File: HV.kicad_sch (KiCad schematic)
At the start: 7 parts, among them J401 1935161, J402 1935161, Q401 MCB90N12A-TP, U401 LTV-816S

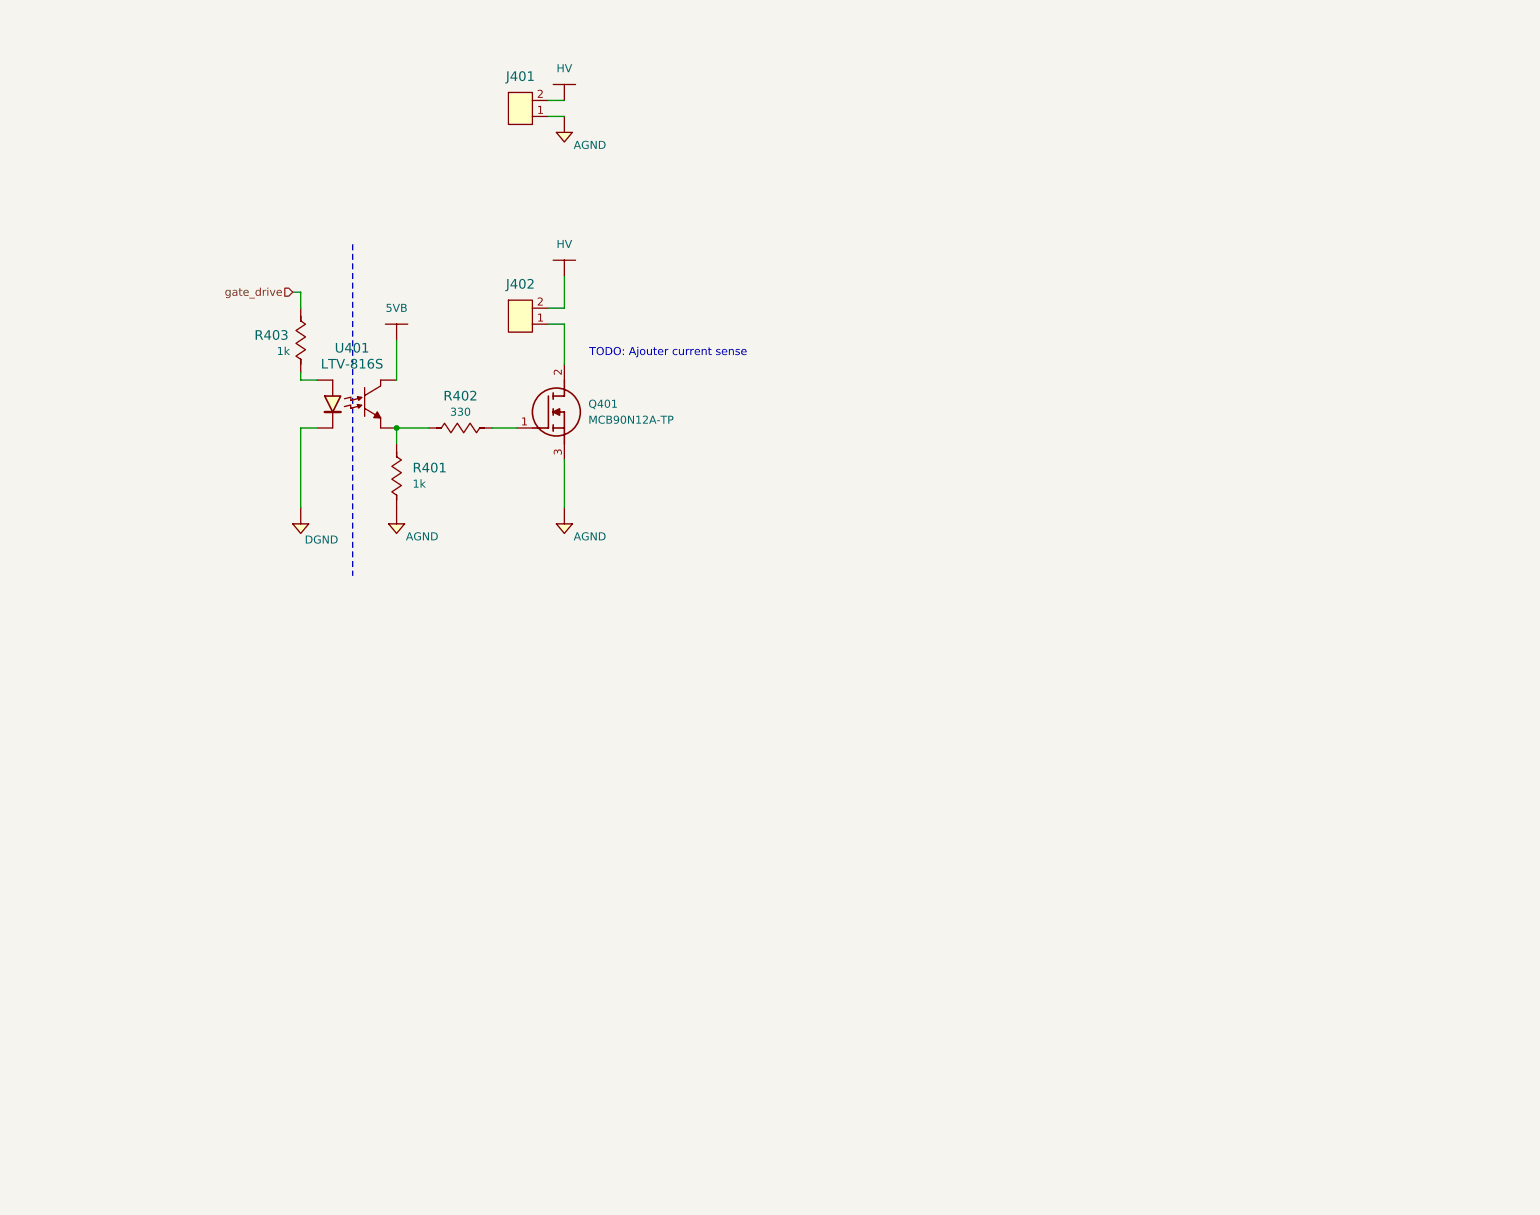
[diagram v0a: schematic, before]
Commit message: update schematic
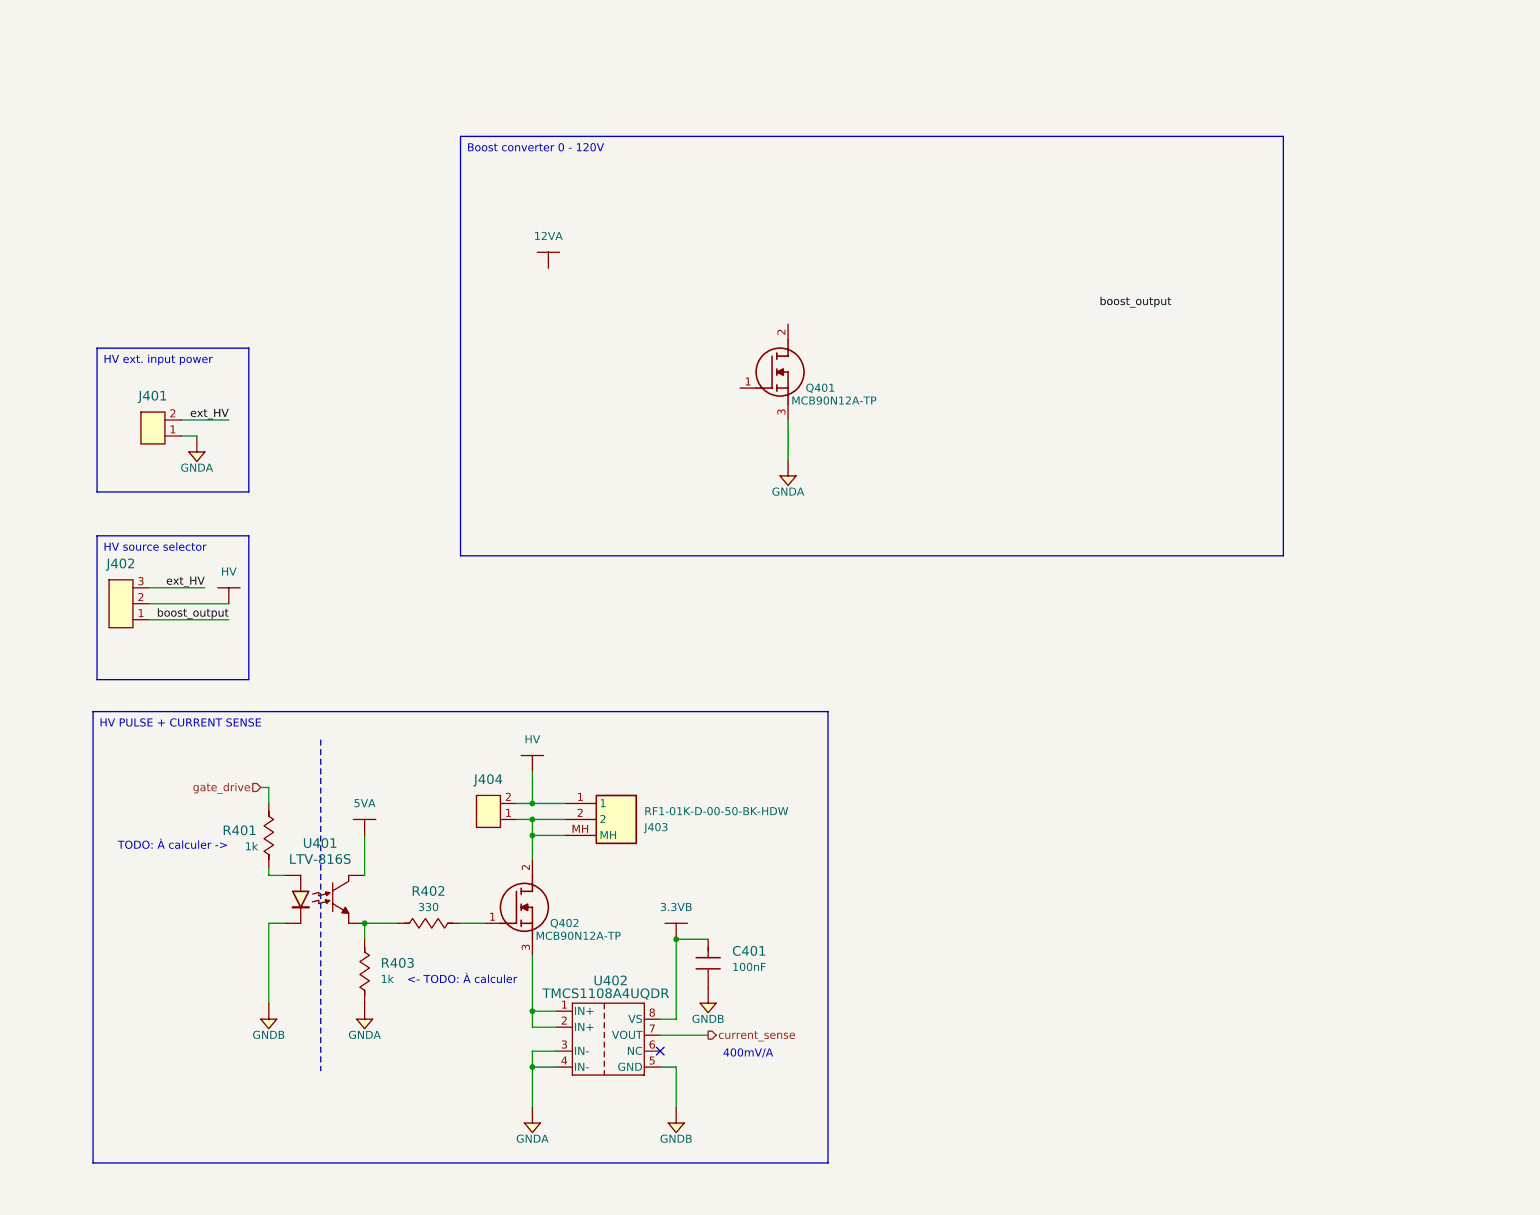
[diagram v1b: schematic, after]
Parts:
- added C401: 885012207098, Capacitors:C0805, symbol Capacitors:885012207098
- added J402: Header_Male_Pin_2.54mm_1X3_,_Unshrouded, Connectors:Headers_2.54mm_1X3, symbol Connectors:Header_Male_Pin_2.54mm_1X3_,_Unshrouded
- added J403: RF1-01K-D-00-50-BK-HDW, Connectors:RF101KD0050, symbol Connectors:RF1-01K-D-00-50-BK-HDW
- added Q401: MCB90N12A-TP, IC:MCB90N12ATP, symbol Transistors:MCB90N12A-TP
- added U402: TMCS1108A4UQDR, IC:SOIC-8, symbol Sensors:TMCS1108A4UQDR
- renumbered J402 to J404, Q401 to Q402, R403 to R401, R401 to R403
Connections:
- net HV: now also J402.2, J403.1; no longer J401.2
- net at J404.1, Q402.2 (D): now also J403.2, J403.MH
- net 5VB renamed 5VA
- net AGND renamed GNDA
- net GNDA: now also Q401.3 (S), U402.3 (IN-), U402.4 (IN-); no longer Q402.3 (S)
- net DGND renamed GNDB
- net GNDB: now also C401.1, U402.5 (GND)
- new net: Q402.3 (S), U402.1 (IN+), U402.2 (IN+)
- new net 3.3VB: C401.2, U402.8 (VS)
- new net boost_output: J402.1
- new net current_sense: U402.7 (VOUT)
- new net ext_HV: J401.2, J402.3
- no-connect marks 0 -> 1
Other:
- note added: "400mV/A"
- note added: "<- TODO: À calculer"
- note added: "TODO: À calculer ->"
- note removed: "TODO: Ajouter current sense"
- title: (none) -> HV
- moved on the sheet: J401, J404, Q402, R401, R402, R403, U401

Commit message: update schematic
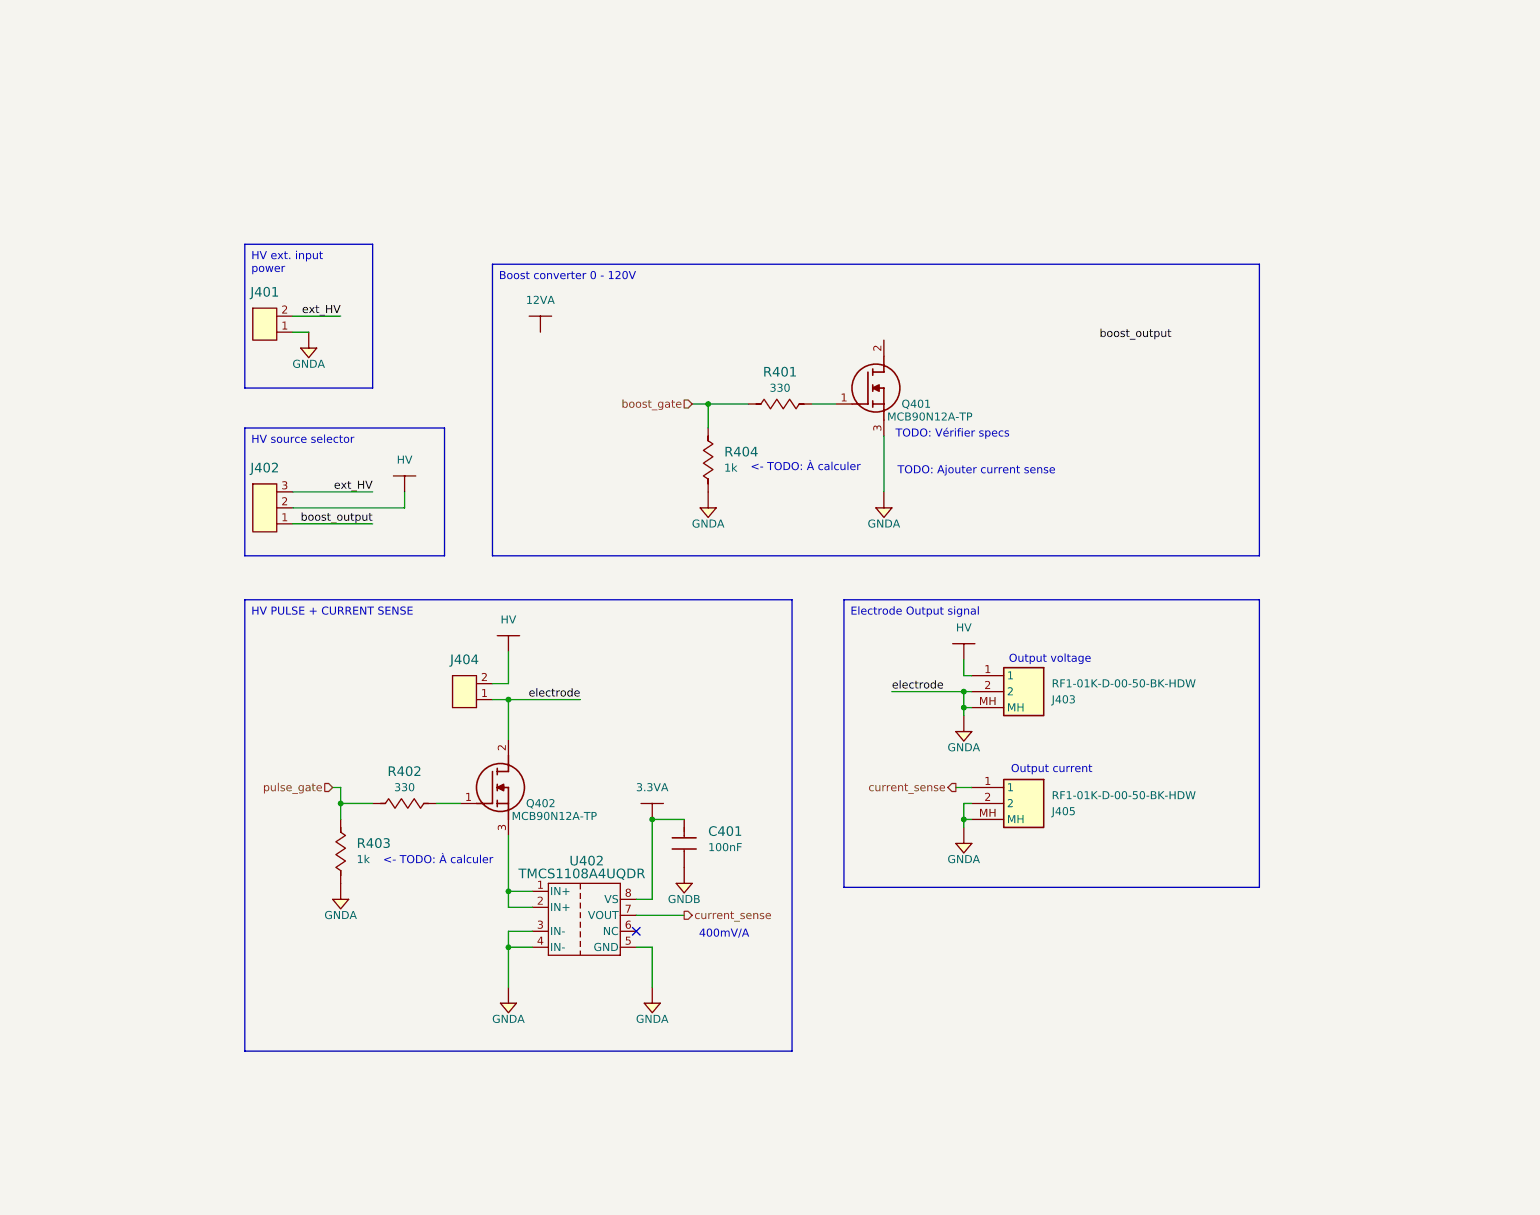
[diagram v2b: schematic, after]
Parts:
- removed R401: RC0805JR-071KL, Resistors:R0805, symbol Resistors:RC0805JR-071KL
- removed U401: LTV-816S, IC:4-SMD, symbol Isolators:LTV-816S
- added J405: RF1-01K-D-00-50-BK-HDW, Connectors:RF101KD0050, symbol Connectors:RF1-01K-D-00-50-BK-HDW
- added R401: RC0805JR-07330RL, Resistors:R0805, symbol Resistors:RC0805JR-07330RL
- added R404: RC0805JR-071KL, Resistors:R0805, symbol Resistors:RC0805JR-071KL
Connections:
- net GNDA: now also J403.2, J403.MH, J404.1, Q402.2 (D), U402.5 (GND), J405.2, J405.MH, R404.1
- net GNDB: no longer U402.5 (GND)
- net current_sense: now also J405.1
- net pulse_gate: now reaches R402.1, R403.2
- net at Q401.1 (G): now also R401.2
- net 3.3VB renamed 3.3VA
- new net boost_gate: R401.1, R404.2
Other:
- note added: "Output current"
- note added: "Output voltage"
- note added: "TODO: Ajouter current sense"
- note added: "TODO: Vérifier specs"
- note removed: "TODO: À calculer ->"
- moved on the sheet: C401, J401, J402, J404, Q401, Q402, R402, R403, U402

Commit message: update schematic
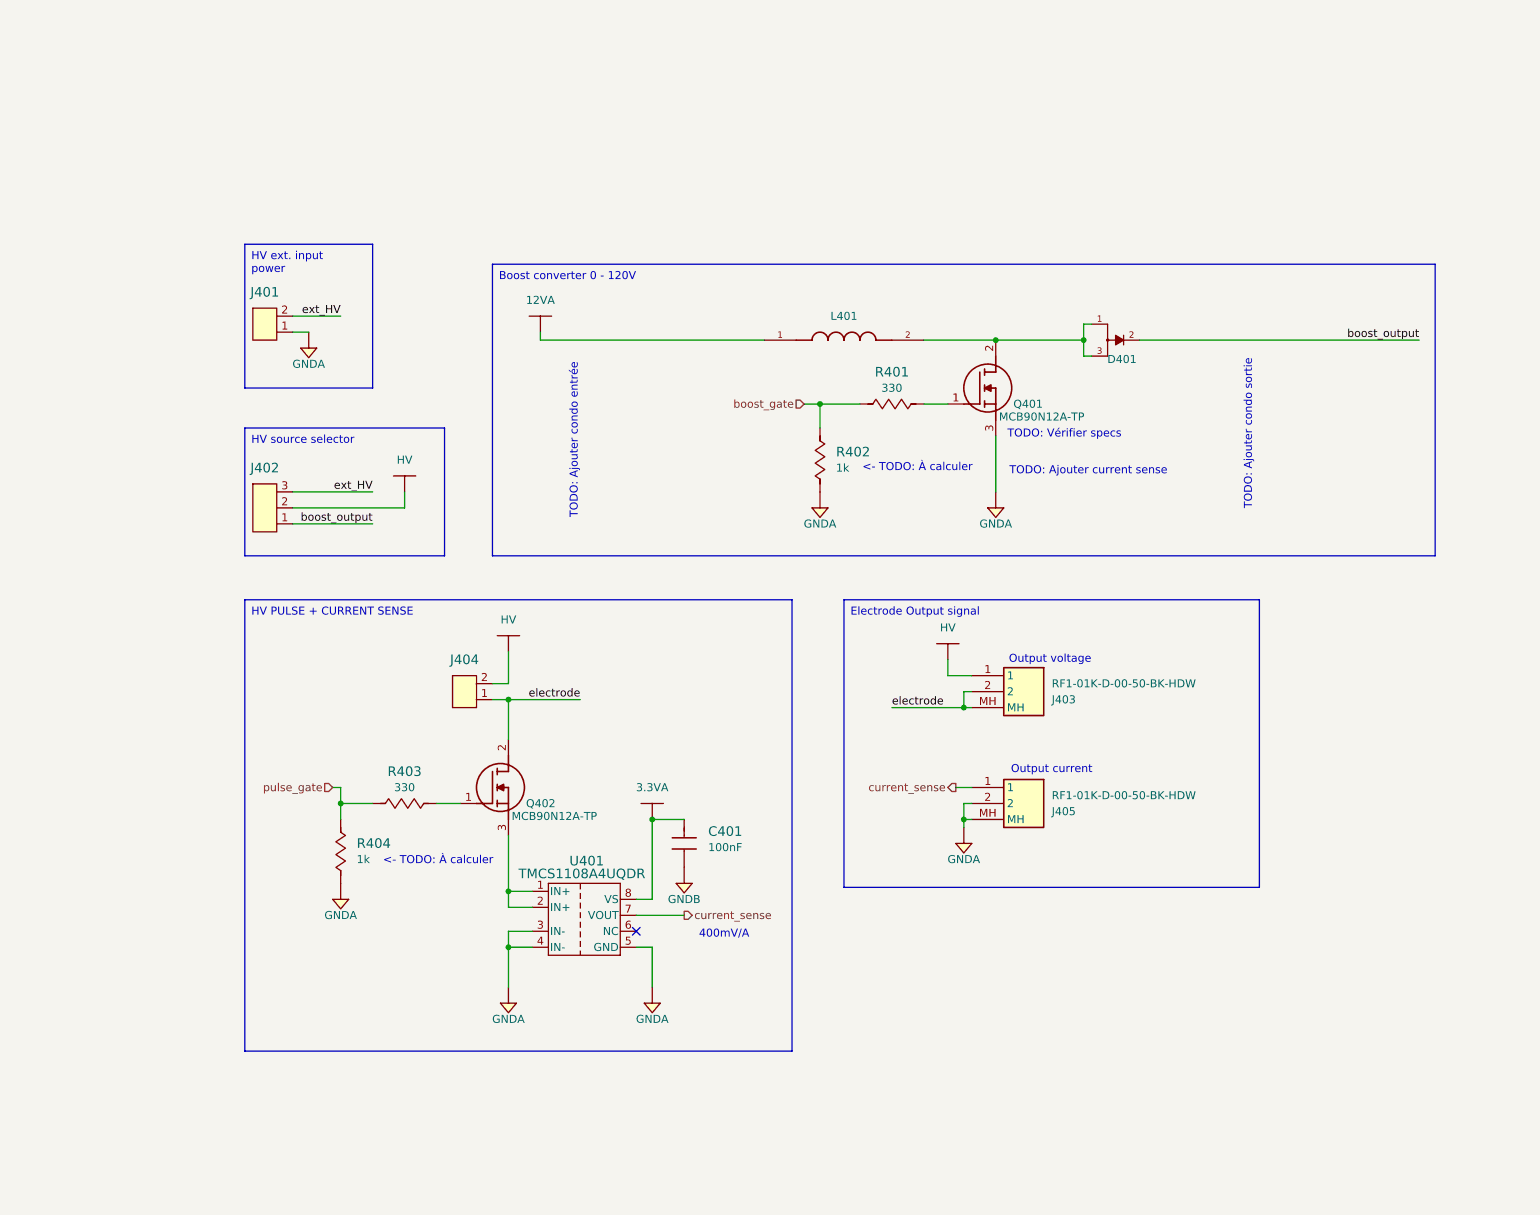
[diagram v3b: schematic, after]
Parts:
- added D401: SBRD10200TR, Diodes:DPAK228P1005X240-4N, symbol Diodes:SBRD10200TR
- added L401: ATCA-08-471M-H, Inductors:IND_ATCA-08-471M-H, symbol Inductors:ATCA-08-471M-H
- renumbered R404 to R402, R402 to R403, R403 to R404, U402 to U401
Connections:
- net 12VA: now also L401.1
- net GNDA: no longer J403.2, J403.MH, J404.1, Q402.2 (D)
- net boost_output: now also D401.2
- net at Q401.2 (D): now also D401.1, D401.3, L401.2
- new net electrode: J403.2, J403.MH, J404.1, Q402.2 (D)
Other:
- note added: "TODO: Ajouter condo entrée"
- note added: "TODO: Ajouter condo sortie"
- moved on the sheet: Q401, R401, R402

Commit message: modif schématique
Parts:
- added D401: SBRD10200TR, Diodes:DPAK228P1005X240-4N, symbol Diodes:SBRD10200TR
- added R403, R411: RMCF0805FT10M0, Resistors:R0805, symbol Resistors:RMCF0805FT10M0
- added R404, R405, R410, R412: RC0805FR-075K6L, Resistors:R0805, symbol Resistors:RC0805FR-075K6L
- added R406, R413: RC0805FR-07200KL, Resistors:R0805, symbol Resistors:RC0805FR-07200KL
- added R408: RC0805JR-071KL, Resistors:R0805, symbol Resistors:RC0805JR-071KL
- added TP401: Test_Point_THM, Connectors:Keystone_5001, symbol Connectors:Test_Point_THM
- added U401: MCP6L04T-E/SL, IC:SOIC127P600X175-14N, symbol Amplifiers:MCP6L04T-E/SL
- added U402: LTV-816S, IC:4-SMD, symbol Isolators:LTV-816S
- D402: renamed from D401; now not fitted
- renumbered J404 to J403, J403 to J404, R403 to R407, R404 to R409, U401 to U403
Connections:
- net 3.3VA: now also U401.4, U402.4 (C)
- net GNDA: now also C401.1, J404.2, J404.MH, R404.2, R406.1, R413.1, U401.11
- net GNDB: now also R408.1; no longer C401.1
- net HV: now also R403.2; no longer J404.1
- net boost_gate: no longer R401.1, R402.2
- net boost_output: now also D401.2, TP401.1 (TP)
- net pulse_gate: now also U402.1 (Anode); no longer R407.1, R409.2
- net at D402.1, D402.3, L401.2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: now also D401.1, D401.3
- net electrode renamed e-
- net e-: now also R411.2; no longer J404.2, J404.MH
- new net: R408.2, U402.2 (Cathode)
- new net: R407.1, R409.2, U402.3 (E)
- new net: R405.1, U401.1, U401.2
- new net: R404.1, R405.2, U401.10
- new net: R411.1, R413.2, U401.5
- new net: R412.1, U401.6, U401.7
- new net: R403.1, R406.2, U401.3
- new net: R401.1, R402.2
- new net: R410.1, R412.2, U401.9
- new net V_amp: J404.1, R410.2, U401.8
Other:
- note added: "TODO: Ajouter fuse à l'entrée"
- note added: "TODO: Ajouter isolation ->"
- note added: "TODO: changer res pour 0.01%"
- note added: "TODO: trouver meilleur current sense"
- moved on the sheet: C401, J401, J402, J403, J404, J405, L401, Q401, Q402, R401, R402, R407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

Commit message: update schematique
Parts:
- removed D402: SBRD10200TR, Diodes:DPAK228P1005X240-4N, symbol Diodes:SBRD10200TR
- removed R402, R408, R409: RC0805JR-071KL, Resistors:R0805, symbol Resistors:RC0805JR-071KL
- added F3: 0697H9120-01, Fuses:TE5_395, symbol Fuses:0697H9120-01
- added R20, R21: RC0805JR-072K2L, Resistors:R0805, symbol Resistors:RC0805JR-072K2L
- added R24, R25: RC0805FR-075K6L, Resistors:R0805, symbol Resistors:RC0805FR-075K6L
- added U8: LTV-816S, IC:4-SMD, symbol Isolators:LTV-816S
- U?: renamed from U403; value TMCS1108A4UQDR -> TMCS1101A3UQDT; symbol Sensors:TMCS1108A4UQDR -> Sensors:TMCS1101A3UQDT; Manufacturer Texas Instruments -> Texas Instruments; Manufacturer Part Number TMCS1108A4UQDR -> TMCS1101A3UQDT; Supplier Part Number 296-TMCS1108A4UQDRCT-ND -> 296-TMCS1101A3UQDTCT-ND
- renumbered C401 to C23, D401 to D10, J403 to J10, J401 to J6, J402 to J7, J404 to J8, J405 to J9, L401 to L1, Q402 to Q1, Q401 to Q2, R407 to R22, R401 to R26, R403 to R27, R406 to R28, R411 to R29, R413 to R30, R405 to R31, R412 to R32, R404 to R33, R410 to R34, TP401 to TP10, U402 to U6, U401 to U9
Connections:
- net 12VA: now also F3.1; no longer L1.1
- net 3.3VA: no longer U6.4 (C)
- net GNDA: now also R24.1, R25.1
- net GNDB: now also R20.1, R21.1
- net boost_gate: now also U8.1 (Anode)
- net at U6.2 (Cathode): now also R20.2
- net at R22.1, U6.3 (E): now also R25.2
- net at R26.1: now also R24.2, U8.3 (E)
- new net: R21.2, U8.2 (Cathode)
- new net: F3.2, L1.1
- new net 5VA: U6.4 (C), U8.4 (C)
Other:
- note removed: "TODO: Ajouter fuse à l'entrée"
- note removed: "TODO: Ajouter isolation ->"
- moved on the sheet: C23, D10, J10, J6, J7, J8, J9, L1, Q1, Q2, R22, R26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
